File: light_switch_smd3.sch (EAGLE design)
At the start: 17 parts, among them J2 SW1, T1 BT136, U1 LM1117

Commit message: light switch version 6 minor adjustments
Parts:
- removed AC, LAMP: DG306-5.0, myblog_library:DG306-5.0
- added AC+LAMP: DG350-3.5-03P, myblog_library:DG350-3.5-03P
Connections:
- net N$11: now also AC+LAMP.P$2; no longer AC.P1, LAMP.P2
- net N$12: now also AC+LAMP.P$3; no longer AC.P2
- net N$8: now also AC+LAMP.P$1; no longer LAMP.P1
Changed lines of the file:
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@@
 <part name="U$1" library="myblog_library" deviceset="HI-LINK5V-ACDC" device=""/>
 <part name="GND4" library="supply1" deviceset="GND" device=""/>
-<part name="LAMP" library="myblog_library" deviceset="DG306-5.0" device=""/>
-<part name="AC" library="myblog_library" deviceset="DG306-5.0" device=""/>
+<part name="AC+LAMP" library="myblog_library" deviceset="DG350-3.5-03P" device=""/>
 </parts>
 <sheets>
@@
 <instance part="U$1" gate="G$1" x="78.74" y="-5.08"/>
 <instance part="GND4" gate="1" x="91.44" y="5.08"/>
-<instance part="LAMP" gate="G$1" x="144.78" y="35.56"/>
-<instance part="AC" gate="G$1" x="144.78" y="20.32"/>
+<instance part="AC+LAMP" gate="G$1" x="144.78" y="35.56" rot="MR0"/>
 </instances>
 <busses>
@@
 <pinref part="OK1" gate="-1" pin="A2"/>
 <wire x1="93.98" y1="38.1" x2="116.84" y2="38.1" width="0.1524" layer="91"/>
-<wire x1="132.08" y1="38.1" x2="116.84" y2="38.1" width="0.1524" layer="91"/>
+<pinref part="AC+LAMP" gate="G$1" pin="P$1"/>
+<wire x1="116.84" y1="38.1" x2="134.62" y2="38.1" width="0.1524" layer="91"/>
 <junction x="116.84" y="38.1"/>
-<pinref part="LAMP" gate="G$1" pin="P1"/>
 </segment>
 </net>
 <net name="N$11" class="0">
 <segment>
-<wire x1="129.54" y1="33.02" x2="129.54" y2="22.86" width="0.1524" layer="91"/>
 <pinref part="U$1" gate="G$1" pin="AC2"/>
-<wire x1="129.54" y1="22.86" x2="129.54" y2="0" width="0.1524" layer="91"/>
+<wire x1="129.54" y1="33.02" x2="129.54" y2="0" width="0.1524" layer="91"/>
 <wire x1="129.54" y1="0" x2="124.46" y2="0" width="0.1524" layer="91"/>
-<wire x1="132.08" y1="33.02" x2="129.54" y2="33.02" width="0.1524" layer="91"/>
-<wire x1="132.08" y1="22.86" x2="129.54" y2="22.86" width="0.1524" layer="91"/>
-<junction x="129.54" y="22.86"/>
-<pinref part="LAMP" gate="G$1" pin="P2"/>
-<pinref part="AC" gate="G$1" pin="P1"/>
+<pinref part="AC+LAMP" gate="G$1" pin="P$2"/>
+<wire x1="134.62" y1="33.02" x2="129.54" y2="33.02" width="0.1524" layer="91"/>
 </segment>
 </net>
@@
 <pinref part="U$1" gate="G$1" pin="AC1"/>
 <wire x1="127" y1="7.62" x2="124.46" y2="7.62" width="0.1524" layer="91"/>
+<pinref part="AC+LAMP" gate="G$1" pin="P$3"/>
+<wire x1="134.62" y1="27.94" x2="132.08" y2="27.94" width="0.1524" layer="91"/>
+<wire x1="132.08" y1="27.94" x2="132.08" y2="17.78" width="0.1524" layer="91"/>
 <wire x1="132.08" y1="17.78" x2="127" y2="17.78" width="0.1524" layer="91"/>
 <junction x="127" y="17.78"/>
-<pinref part="AC" gate="G$1" pin="P2"/>
 </segment>
 </net>

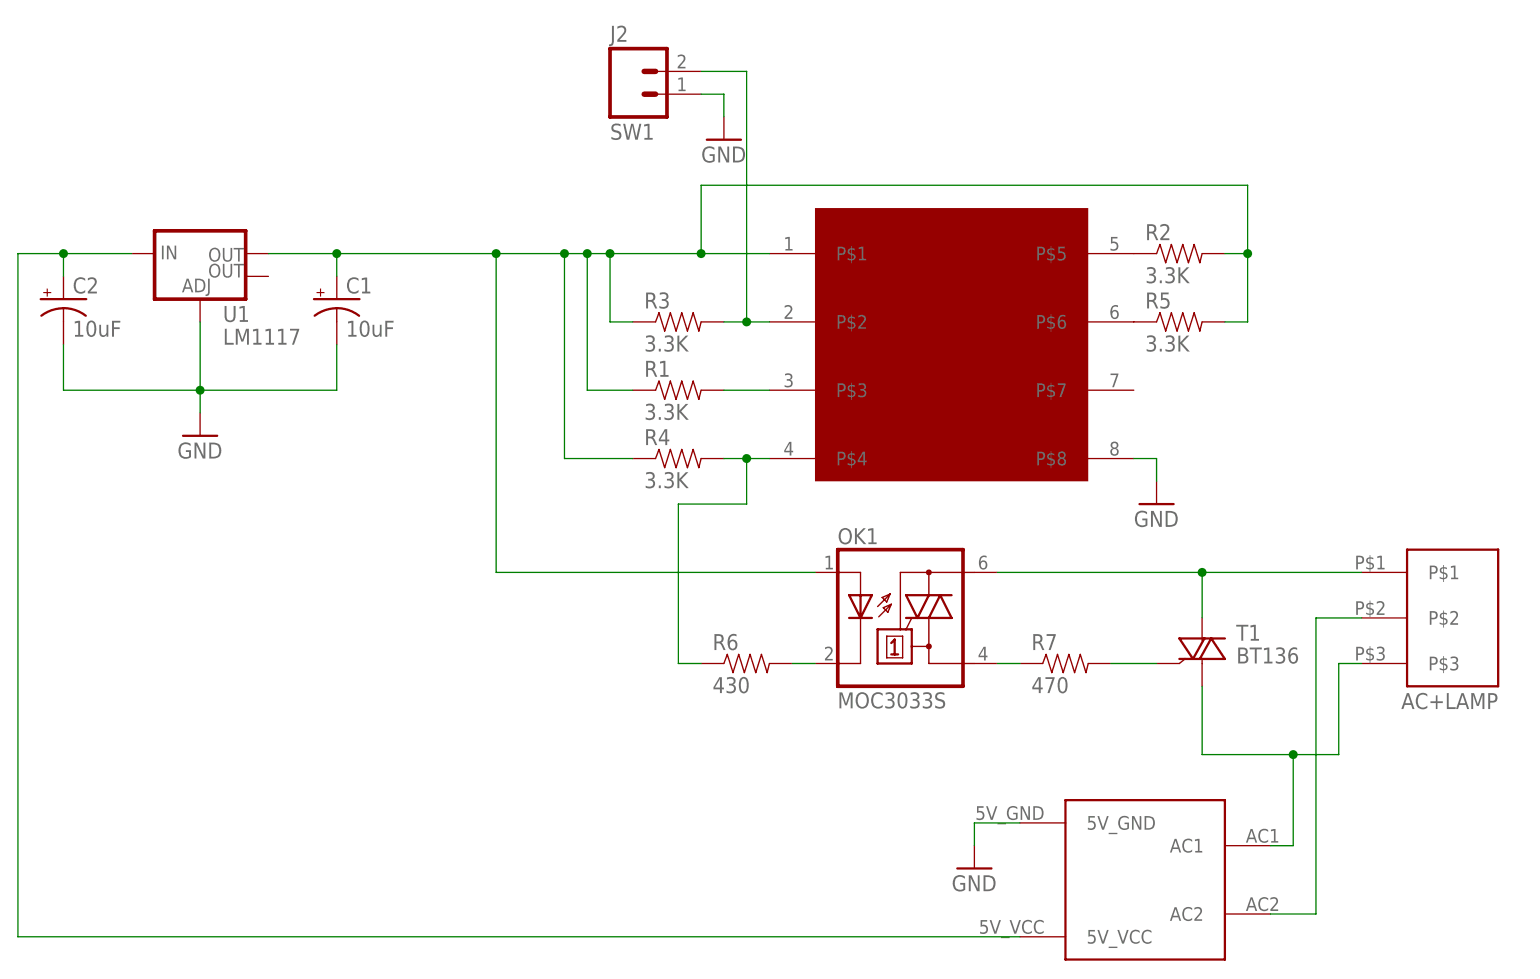
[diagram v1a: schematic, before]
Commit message: Changing the BT136 device
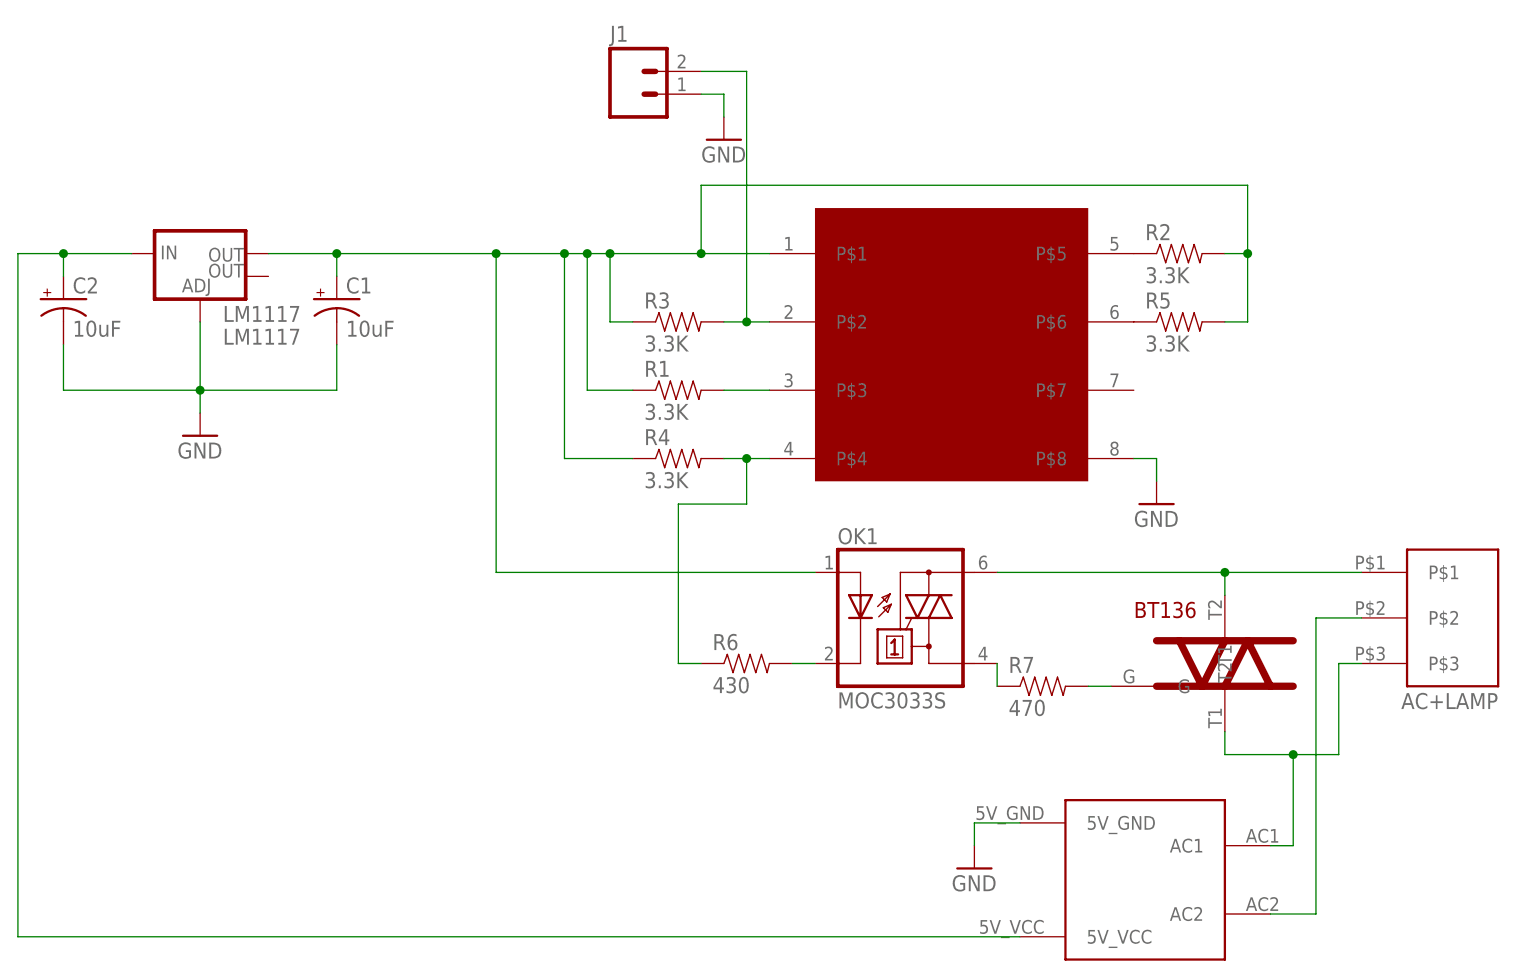
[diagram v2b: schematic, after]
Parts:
- removed J2: SW1, SparkFun-Connectors:M02PTH3
- removed T1: BT136, triac:BT136
- added BT136: BT136, myblog_library:BT136
- added J1: (no value), SparkFun-Connectors:M02PTH
- renumbered U1 to LM1117
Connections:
- net GND: now also J1.1; no longer J2.1
- net N$1: now also J1.2; no longer J2.2
- net N$12: now also BT136.T1; no longer T1.A1
- net N$6: now also BT136.G; no longer T1.G
- net N$8: now also BT136.T2; no longer T1.A2
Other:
- moved on the sheet: R7
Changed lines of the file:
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@@
 </classes>
 <parts>
-<part name="U1" library="SparkFun-PowerIC" deviceset="V_REG_LM1117" device="SOT223" value="LM1117"/>
+<part name="LM1117" library="SparkFun-PowerIC" deviceset="V_REG_LM1117" device="SOT223" value="LM1117"/>
 <part name="C1" library="SparkFun-Capacitors" deviceset="10UF-16V-10%(TANT)" device="" value="10uF"/>
 <part name="C2" library="SparkFun-Capacitors" deviceset="10UF-16V-10%(TANT)" device="" value="10uF"/>
@@
 <part name="GND1" library="supply1" deviceset="GND" device=""/>
 <part name="GND2" library="supply1" deviceset="GND" device=""/>
-<part name="J2" library="SparkFun-Connectors" deviceset="M02" device="PTH3" value="SW1"/>
 <part name="GND3" library="supply1" deviceset="GND" device=""/>
-<part name="T1" library="triac" deviceset="BT136" device=""/>
 <part name="OK1" library="optocoupler" deviceset="MOC30*" device="S" technology="33"/>
 <part name="U$2" library="myblog_library" deviceset="ESP8266-01" device=""/>
@@
 <part name="GND4" library="supply1" deviceset="GND" device=""/>
 <part name="AC+LAMP" library="myblog_library" deviceset="DG350-3.5-03P" device=""/>
+<part name="J1" library="SparkFun-Connectors" deviceset="M02" device="PTH"/>
+<part name="BT136" library="myblog_library" deviceset="BT136" device=""/>
 </parts>
 <sheets>
@@
 </plain>
 <instances>
-<instance part="U1" gate="G$1" x="5.08" y="73.66"/>
+<instance part="LM1117" gate="G$1" x="5.08" y="73.66"/>
 <instance part="C1" gate="G$1" x="20.32" y="68.58"/>
 <instance part="C2" gate="G$1" x="-10.16" y="68.58"/>
@@
 <instance part="R5" gate="G$1" x="114.3" y="66.04"/>
 <instance part="R6" gate="G$1" x="66.04" y="27.94"/>
-<instance part="R7" gate="G$1" x="101.6" y="27.94"/>
+<instance part="R7" gate="G$1" x="99.06" y="25.4"/>
 <instance part="GND1" gate="1" x="5.08" y="53.34"/>
 <instance part="GND2" gate="1" x="111.76" y="45.72"/>
-<instance part="J2" gate="G$1" x="53.34" y="91.44"/>
 <instance part="GND3" gate="1" x="63.5" y="86.36"/>
-<instance part="T1" gate="-1" x="116.84" y="27.94"/>
 <instance part="OK1" gate="-1" x="83.82" y="33.02"/>
 <instance part="U$2" gate="G$1" x="88.9" y="63.5"/>
@@
 <instance part="GND4" gate="1" x="91.44" y="5.08"/>
 <instance part="AC+LAMP" gate="G$1" x="144.78" y="35.56" rot="MR0"/>
+<instance part="J1" gate="G$1" x="53.34" y="91.44"/>
+<instance part="BT136" gate="G$1" x="119.38" y="27.94"/>
 </instances>
 <busses>
@@
 </segment>
 <segment>
-<pinref part="J2" gate="G$1" pin="1"/>
-<wire x1="60.96" y1="91.44" x2="63.5" y2="91.44" width="0.1524" layer="91"/>
-<pinref part="GND3" gate="1" pin="GND"/>
-<wire x1="63.5" y1="91.44" x2="63.5" y2="88.9" width="0.1524" layer="91"/>
-</segment>
-<segment>
-<pinref part="U1" gate="G$1" pin="ADJ"/>
+<pinref part="LM1117" gate="G$1" pin="ADJ"/>
 <pinref part="GND1" gate="1" pin="GND"/>
 <wire x1="5.08" y1="66.04" x2="5.08" y2="58.42" width="0.1524" layer="91"/>
@@
 <wire x1="91.44" y1="10.16" x2="91.44" y2="7.62" width="0.1524" layer="91"/>
 </segment>
+<segment>
+<pinref part="J1" gate="G$1" pin="1"/>
+<pinref part="GND3" gate="1" pin="GND"/>
+<wire x1="60.96" y1="91.44" x2="63.5" y2="91.44" width="0.1524" layer="91"/>
+<wire x1="63.5" y1="91.44" x2="63.5" y2="88.9" width="0.1524" layer="91"/>
+</segment>
 </net>
 <net name="N$3" class="0">
 <segment>
-<pinref part="U1" gate="G$1" pin="OUT"/>
+<pinref part="LM1117" gate="G$1" pin="OUT"/>
 <pinref part="C1" gate="G$1" pin="+"/>
 <wire x1="12.7" y1="73.66" x2="20.32" y2="73.66" width="0.1524" layer="91"/>
@@
 </segment>
 </net>
-<net name="N$6" class="0">
-<segment>
-<pinref part="T1" gate="-1" pin="G"/>
-<pinref part="R7" gate="G$1" pin="2"/>
-<wire x1="111.76" y1="27.94" x2="106.68" y2="27.94" width="0.1524" layer="91"/>
-</segment>
-</net>
 <net name="N$7" class="0">
 <segment>
 <pinref part="OK1" gate="-1" pin="A1"/>
 <pinref part="R7" gate="G$1" pin="1"/>
-<wire x1="93.98" y1="27.94" x2="96.52" y2="27.94" width="0.1524" layer="91"/>
+<wire x1="93.98" y1="27.94" x2="93.98" y2="25.4" width="0.1524" layer="91"/>
 </segment>
 </net>
 <net name="N$8" class="0">
 <segment>
-<pinref part="T1" gate="-1" pin="A2"/>
-<wire x1="116.84" y1="33.02" x2="116.84" y2="38.1" width="0.1524" layer="91"/>
 <pinref part="OK1" gate="-1" pin="A2"/>
-<wire x1="93.98" y1="38.1" x2="116.84" y2="38.1" width="0.1524" layer="91"/>
+<wire x1="93.98" y1="38.1" x2="119.38" y2="38.1" width="0.1524" layer="91"/>
 <pinref part="AC+LAMP" gate="G$1" pin="P$1"/>
-<wire x1="116.84" y1="38.1" x2="134.62" y2="38.1" width="0.1524" layer="91"/>
-<junction x="116.84" y="38.1"/>
+<pinref part="BT136" gate="G$1" pin="T2"/>
+<wire x1="119.38" y1="38.1" x2="134.62" y2="38.1" width="0.1524" layer="91"/>
+<wire x1="119.38" y1="35.56" x2="119.38" y2="38.1" width="0.1524" layer="91"/>
+<junction x="119.38" y="38.1"/>
 </segment>
 </net>
@@
 <net name="N$12" class="0">
 <segment>
-<pinref part="T1" gate="-1" pin="A1"/>
-<wire x1="116.84" y1="25.4" x2="116.84" y2="17.78" width="0.1524" layer="91"/>
-<wire x1="116.84" y1="17.78" x2="127" y2="17.78" width="0.1524" layer="91"/>
 <wire x1="127" y1="17.78" x2="127" y2="7.62" width="0.1524" layer="91"/>
 <pinref part="U$1" gate="G$1" pin="AC1"/>
@@
 <wire x1="132.08" y1="27.94" x2="132.08" y2="17.78" width="0.1524" layer="91"/>
 <wire x1="132.08" y1="17.78" x2="127" y2="17.78" width="0.1524" layer="91"/>
+<pinref part="BT136" gate="G$1" pin="T1"/>
+<wire x1="119.38" y1="20.32" x2="119.38" y2="17.78" width="0.1524" layer="91"/>
+<wire x1="119.38" y1="17.78" x2="127" y2="17.78" width="0.1524" layer="91"/>
 <junction x="127" y="17.78"/>
 </segment>
@@
 <net name="N$13" class="0">
 <segment>
-<pinref part="U1" gate="G$1" pin="IN"/>
+<pinref part="LM1117" gate="G$1" pin="IN"/>
 <pinref part="C2" gate="G$1" pin="+"/>
 <wire x1="-2.54" y1="73.66" x2="-10.16" y2="73.66" width="0.1524" layer="91"/>
@@
 <net name="N$1" class="0">
 <segment>
-<pinref part="J2" gate="G$1" pin="2"/>
-<wire x1="60.96" y1="93.98" x2="66.04" y2="93.98" width="0.1524" layer="91"/>
 <pinref part="U$2" gate="G$1" pin="P$2"/>
 <pinref part="R3" gate="G$1" pin="2"/>
 <wire x1="63.5" y1="66.04" x2="66.04" y2="66.04" width="0.1524" layer="91"/>
+<pinref part="J1" gate="G$1" pin="2"/>
 <wire x1="66.04" y1="66.04" x2="68.58" y2="66.04" width="0.1524" layer="91"/>
+<wire x1="60.96" y1="93.98" x2="66.04" y2="93.98" width="0.1524" layer="91"/>
 <wire x1="66.04" y1="93.98" x2="66.04" y2="66.04" width="0.1524" layer="91"/>
 <junction x="66.04" y="66.04"/>
@@
 </segment>
 </net>
+<net name="N$6" class="0">
+<segment>
+<pinref part="R7" gate="G$1" pin="2"/>
+<pinref part="BT136" gate="G$1" pin="G"/>
+<wire x1="104.14" y1="25.4" x2="106.68" y2="25.4" width="0.1524" layer="91"/>
+</segment>
+</net>

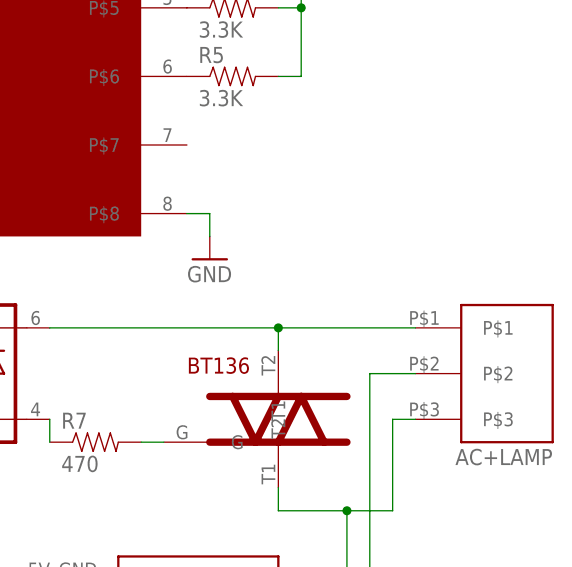
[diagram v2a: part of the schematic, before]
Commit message: Rev. 0.7 - Light Switch is minified and the silkscreen is cleared
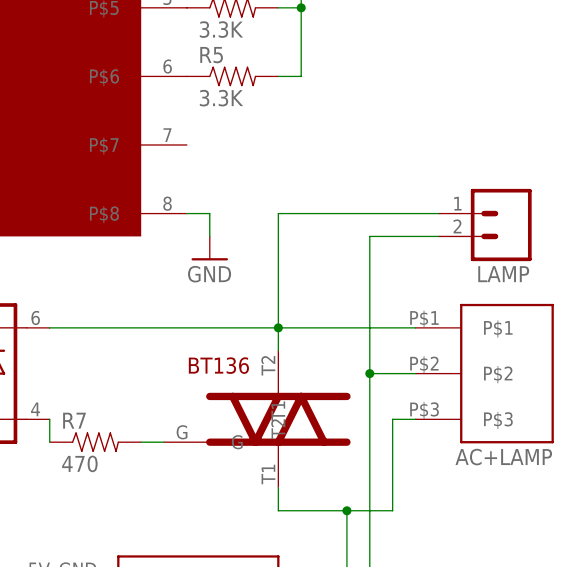
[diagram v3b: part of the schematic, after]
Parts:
- added LAMP: (no value), SparkFun-Connectors:M02PTH
- C1, C2: device SparkFun-Capacitors:10UF-16V-10%(TANT) -> SparkFun-Capacitors:10UF-6.3V-20%(0603)(TANT)"
- R1, R2, R3, R4, R5: device SparkFun-Resistors:RESISTOR1206 -> SparkFun-Resistors:3.3MOHM-1/10W-1%(0603)
- R6, R7: device SparkFun-Resistors:RESISTOR1206 -> SparkFun-Resistors:RESISTOR0603
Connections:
- net N$11: now also LAMP.2
- net N$8: now also LAMP.1
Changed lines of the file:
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@@
 <parts>
 <part name="LM1117" library="SparkFun-PowerIC" deviceset="V_REG_LM1117" device="SOT223" value="LM1117"/>
-<part name="C1" library="SparkFun-Capacitors" deviceset="10UF-16V-10%(TANT)" device="" value="10uF"/>
-<part name="C2" library="SparkFun-Capacitors" deviceset="10UF-16V-10%(TANT)" device="" value="10uF"/>
-<part name="R1" library="SparkFun-Resistors" deviceset="RESISTOR" device="1206" value="3.3K"/>
-<part name="R2" library="SparkFun-Resistors" deviceset="RESISTOR" device="1206" value="3.3K"/>
-<part name="R3" library="SparkFun-Resistors" deviceset="RESISTOR" device="1206" value="3.3K"/>
-<part name="R4" library="SparkFun-Resistors" deviceset="RESISTOR" device="1206" value="3.3K"/>
-<part name="R5" library="SparkFun-Resistors" deviceset="RESISTOR" device="1206" value="3.3K"/>
-<part name="R6" library="SparkFun-Resistors" deviceset="RESISTOR" device="1206" value="430"/>
-<part name="R7" library="SparkFun-Resistors" deviceset="RESISTOR" device="1206" value="470"/>
+<part name="C1" library="SparkFun-Capacitors" deviceset="10UF-6.3V-20%(0603)(TANT)" device="&quot;" value="10uF"/>
+<part name="C2" library="SparkFun-Capacitors" deviceset="10UF-6.3V-20%(0603)(TANT)" device="&quot;" value="10uF"/>
+<part name="R1" library="SparkFun-Resistors" deviceset="3.3MOHM-1/10W-1%(0603)" device="" value="3.3K"/>
+<part name="R2" library="SparkFun-Resistors" deviceset="3.3MOHM-1/10W-1%(0603)" device="" value="3.3K"/>
+<part name="R3" library="SparkFun-Resistors" deviceset="3.3MOHM-1/10W-1%(0603)" device="" value="3.3K"/>
+<part name="R4" library="SparkFun-Resistors" deviceset="3.3MOHM-1/10W-1%(0603)" device="" value="3.3K"/>
+<part name="R5" library="SparkFun-Resistors" deviceset="3.3MOHM-1/10W-1%(0603)" device="" value="3.3K"/>
+<part name="R6" library="SparkFun-Resistors" deviceset="RESISTOR" device="0603" value="430"/>
+<part name="R7" library="SparkFun-Resistors" deviceset="RESISTOR" device="0603" value="470"/>
 <part name="GND1" library="supply1" deviceset="GND" device=""/>
 <part name="GND2" library="supply1" deviceset="GND" device=""/>
@@
 <part name="J1" library="SparkFun-Connectors" deviceset="M02" device="PTH"/>
 <part name="BT136" library="myblog_library" deviceset="BT136" device=""/>
+<part name="LAMP" library="SparkFun-Connectors" deviceset="M02" device="PTH"/>
 </parts>
 <sheets>
@@
 <instance part="J1" gate="G$1" x="53.34" y="91.44"/>
 <instance part="BT136" gate="G$1" x="119.38" y="27.94"/>
+<instance part="LAMP" gate="G$1" x="144.78" y="50.8" rot="R180"/>
 </instances>
 <busses>
@@
 <wire x1="93.98" y1="38.1" x2="119.38" y2="38.1" width="0.1524" layer="91"/>
 <pinref part="AC+LAMP" gate="G$1" pin="P$1"/>
+<pinref part="LAMP" gate="G$1" pin="1"/>
+<wire x1="119.38" y1="38.1" x2="134.62" y2="38.1" width="0.1524" layer="91"/>
+<wire x1="137.16" y1="50.8" x2="119.38" y2="50.8" width="0.1524" layer="91"/>
+<wire x1="119.38" y1="50.8" x2="119.38" y2="38.1" width="0.1524" layer="91"/>
 <pinref part="BT136" gate="G$1" pin="T2"/>
-<wire x1="119.38" y1="38.1" x2="134.62" y2="38.1" width="0.1524" layer="91"/>
 <wire x1="119.38" y1="35.56" x2="119.38" y2="38.1" width="0.1524" layer="91"/>
 <junction x="119.38" y="38.1"/>
@@
 <pinref part="AC+LAMP" gate="G$1" pin="P$2"/>
 <wire x1="134.62" y1="33.02" x2="129.54" y2="33.02" width="0.1524" layer="91"/>
+<pinref part="LAMP" gate="G$1" pin="2"/>
+<wire x1="137.16" y1="48.26" x2="129.54" y2="48.26" width="0.1524" layer="91"/>
+<wire x1="129.54" y1="48.26" x2="129.54" y2="33.02" width="0.1524" layer="91"/>
+<junction x="129.54" y="33.02"/>
 </segment>
 </net>
